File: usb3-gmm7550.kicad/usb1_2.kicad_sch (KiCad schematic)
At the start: 28 parts, among them U6 SN65LVDS4RSER, U7 USB3340, U8 STUSB03E

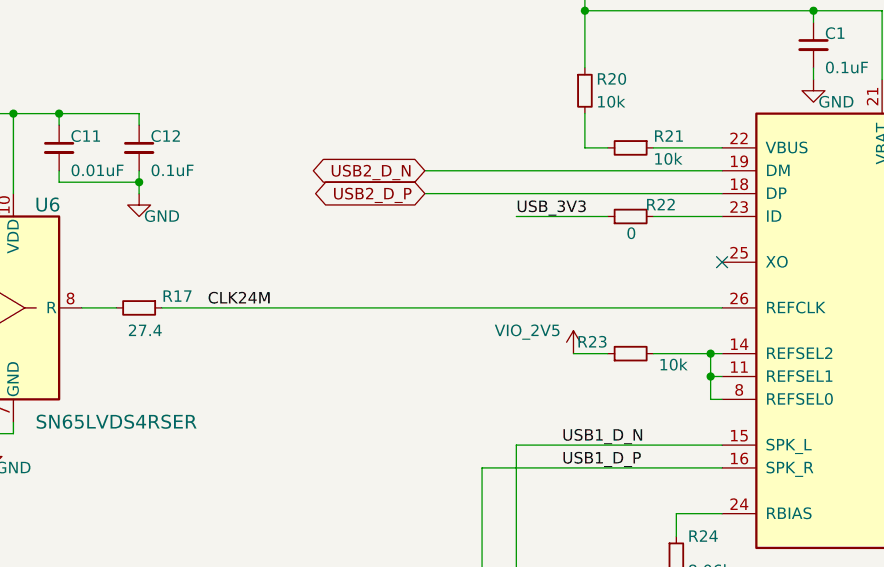
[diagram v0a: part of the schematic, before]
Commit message: Connect USB 3 SuperSpeed diff. pairs
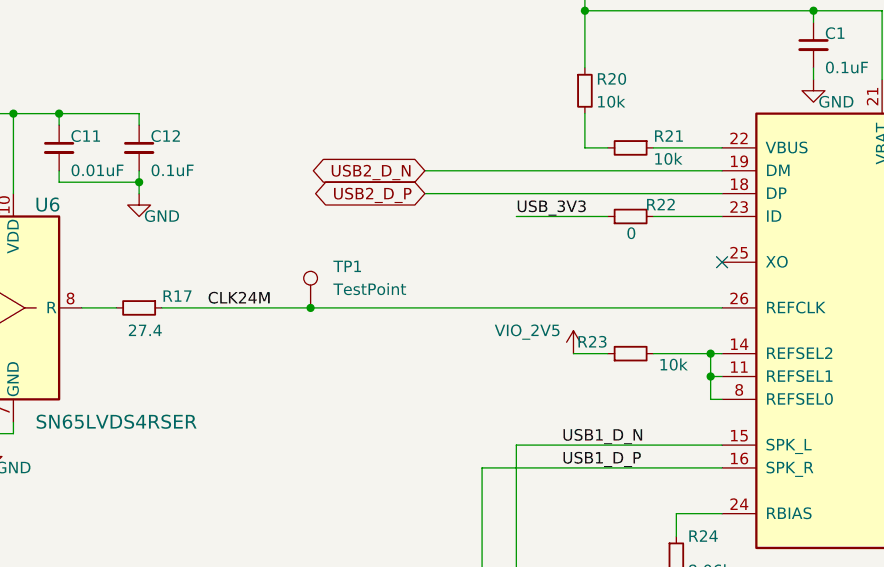
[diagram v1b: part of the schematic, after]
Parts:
- added TP1: TestPoint, TestPoint:TestPoint_Pad_D1.0mm, symbol Connector:TestPoint
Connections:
- net CLK24M: now also TP1.1
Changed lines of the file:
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@@
 	)
 	(junction
+		(at 101.6 59.69)
+		(diameter 0)
+		(color 0 0 0 0)
+	)
+	(junction
 		(at 191.77 82.55)
 		(diameter 0)
@@
 	(wire
 		(pts
+			(xy 101.6 59.69) (xy 147.32 59.69)
+		)
+		(stroke
+			(width 0)
+			(type default)
+		)
+	)
+	(wire
+		(pts
 			(xy 187.96 59.69) (xy 219.71 59.69)
 		)
@@
 	(wire
 		(pts
-			(xy 85.09 59.69) (xy 147.32 59.69)
+			(xy 85.09 59.69) (xy 101.6 59.69)
 		)
 		(stroke
@@
 					(unit 1)
 				)
+			)
+		)
+	)
+	(symbol
+		(lib_id "Connector:TestPoint")
+		(at 101.6 59.69 0)
+		(unit 1)
+		(exclude_from_sim no)
+		(in_bom yes)
+		(on_board yes)
+		(dnp no)
+		(fields_autoplaced yes)
+		(property "Reference" "TP1"
+			(at 104.14 55.1179 0)
+			(effects
+				(font
+					(size 1.27 1.27)
+				)
+				(justify left)
+			)
+		)
+		(property "Value" "TestPoint"
+			(at 104.14 57.6579 0)
+			(effects
+				(font
+					(size 1.27 1.27)
+				)
+				(justify left)
+			)
+		)
+		(property "Footprint" "TestPoint:TestPoint_Pad_D1.0mm"
+			(at 106.68 59.69 0)
+			(effects
+				(font
+					(size 1.27 1.27)
+				)
+				(hide yes)
+			)
+		)
+		(property "Datasheet" "~"
+			(at 106.68 59.69 0)
+			(effects
+				(font
+					(size 1.27 1.27)
+				)
+				(hide yes)
+			)
+		)
+		(property "Description" "test point"
+			(at 101.6 59.69 0)
+			(effects
+				(font
+					(size 1.27 1.27)
+				)
+				(hide yes)
+			)
+		)
+		(pin "1"
+		)
+		(instances
+			(project ""
+				(path "/e63e39d7-6ac0-4ffd-8aa3-1841a4541b55/d7caf9d0-36da-4a2b-bd32-7c05025d3dd2"
+					(reference "TP1")
+					(unit 1)
+				)

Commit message: Layout -- WIP...
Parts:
- added TP2: TestPoint, TestPoint:TestPoint_Pad_D1.0mm, symbol Connector:TestPoint
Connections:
- net ULPI_CLK: now also TP2.1
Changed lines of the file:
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@@
 	)
 	(junction
+		(at 205.74 80.01)
+		(diameter 0)
+		(color 0 0 0 0)
+	)
+	(junction
 		(at 45.72 63.5)
 		(diameter 0)
@@
 	(wire
 		(pts
-			(xy 199.39 80.01) (xy 219.71 80.01)
+			(xy 199.39 80.01) (xy 205.74 80.01)
 		)
 		(stroke
@@
 	(wire
 		(pts
+			(xy 205.74 80.01) (xy 219.71 80.01)
+		)
+		(stroke
+			(width 0)
+			(type default)
+		)
+	)
+	(wire
+		(pts
 			(xy 191.77 82.55) (xy 219.71 82.55)
 		)
@@
 	(wire
 		(pts
+			(xy 205.74 78.74) (xy 205.74 80.01)
+		)
+		(stroke
+			(width 0)
+			(type default)
+		)
+	)
+	(wire
+		(pts
 			(xy 82.55 45.72) (xy 82.55 46.99)
 		)
@@
 					(unit 1)
 				)
+			)
+		)
+	)
+	(symbol
+		(lib_id "Connector:TestPoint")
+		(at 205.74 78.74 270)
+		(unit 1)
+		(exclude_from_sim no)
+		(in_bom yes)
+		(on_board yes)
+		(dnp no)
+		(property "Reference" "TP2"
+			(at 207.01 76.2 90)
+			(effects
+				(font
+					(size 1.27 1.27)
+				)
+				(justify left)
+			)
+		)
+		(property "Value" "TestPoint"
+			(at 207.01 81.28 90)
+			(effects
+				(font
+					(size 1.27 1.27)
+				)
+				(justify left)
+			)
+		)
+		(property "Footprint" "TestPoint:TestPoint_Pad_D1.0mm"
+			(at 205.74 83.82 0)
+			(effects
+				(font
+					(size 1.27 1.27)
+				)
+				(hide yes)
+			)
+		)
+		(property "Datasheet" "~"
+			(at 205.74 83.82 0)
+			(effects
+				(font
+					(size 1.27 1.27)
+				)
+				(hide yes)
+			)
+		)
+		(property "Description" "test point"
+			(at 205.74 78.74 0)
+			(effects
+				(font
+					(size 1.27 1.27)
+				)
+				(hide yes)
+			)
+		)
+		(pin "1"
+		)
+		(instances
+			(project "usb3-gmm7550"
+				(path "/e63e39d7-6ac0-4ffd-8aa3-1841a4541b55/d7caf9d0-36da-4a2b-bd32-7c05025d3dd2"
+					(reference "TP2")
+					(unit 1)
+				)

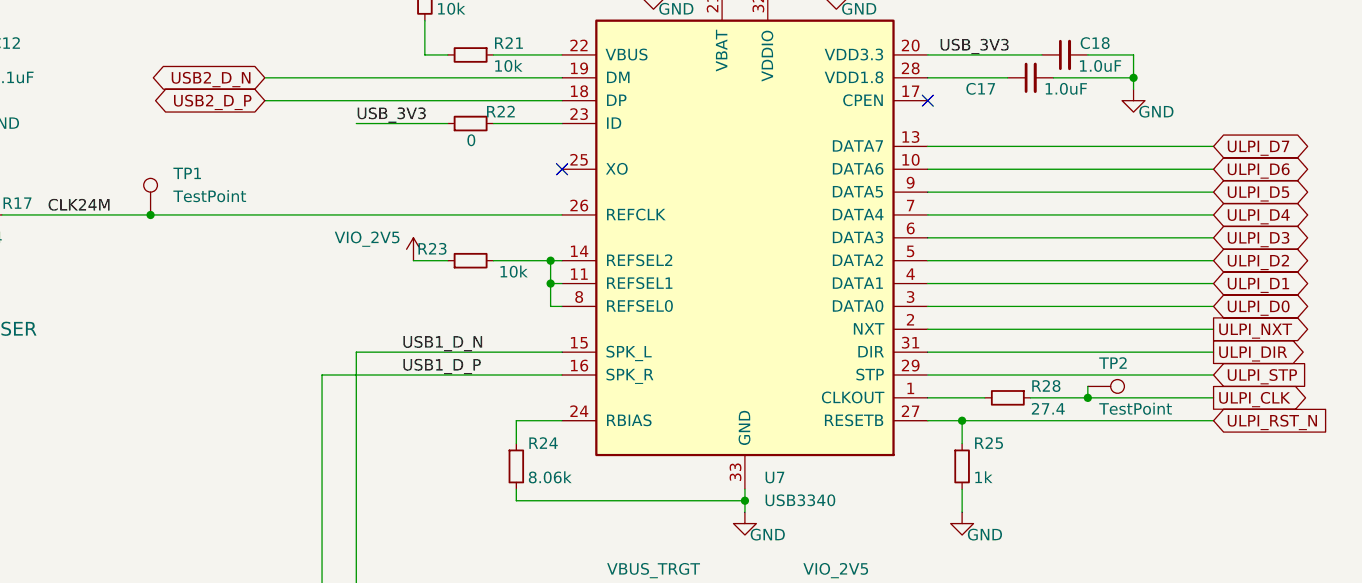
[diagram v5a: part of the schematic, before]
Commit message: Layout [almost] complete -- all connections are routed
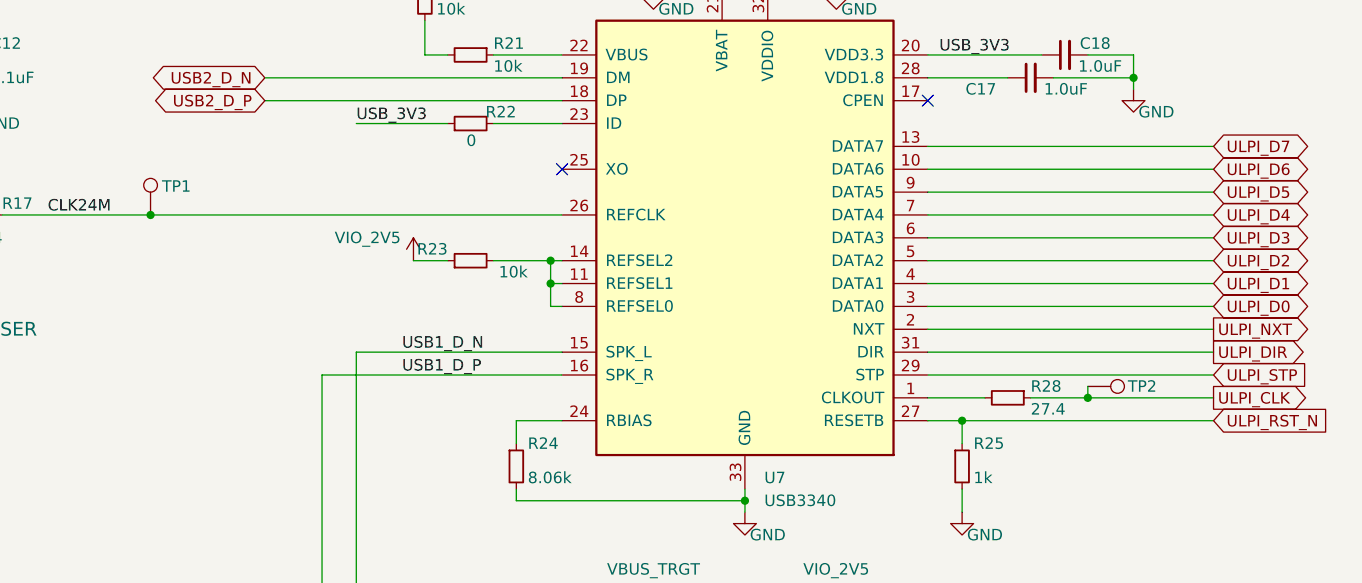
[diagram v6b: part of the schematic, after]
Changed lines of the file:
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@@
 		(dnp no)
 		(property "Reference" "TP2"
-			(at 207.01 76.2 90)
+			(at 210.185 78.74 90)
 			(effects
 				(font
@@
 				)
 				(justify left)
+				(hide yes)
 			)
 		)
@@
 		(on_board yes)
 		(dnp no)
-		(fields_autoplaced yes)
 		(property "Reference" "TP1"
-			(at 104.14 55.1179 0)
+			(at 102.87 56.515 0)
 			(effects
 				(font
@@
 				)
 				(justify left)
-			)
-		)
+				(hide yes)
+			)
+		)
